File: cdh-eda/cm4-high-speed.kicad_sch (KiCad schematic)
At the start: 5 parts, among them J4 USB_OTG, U2 TPD2EUSB30ADRTR

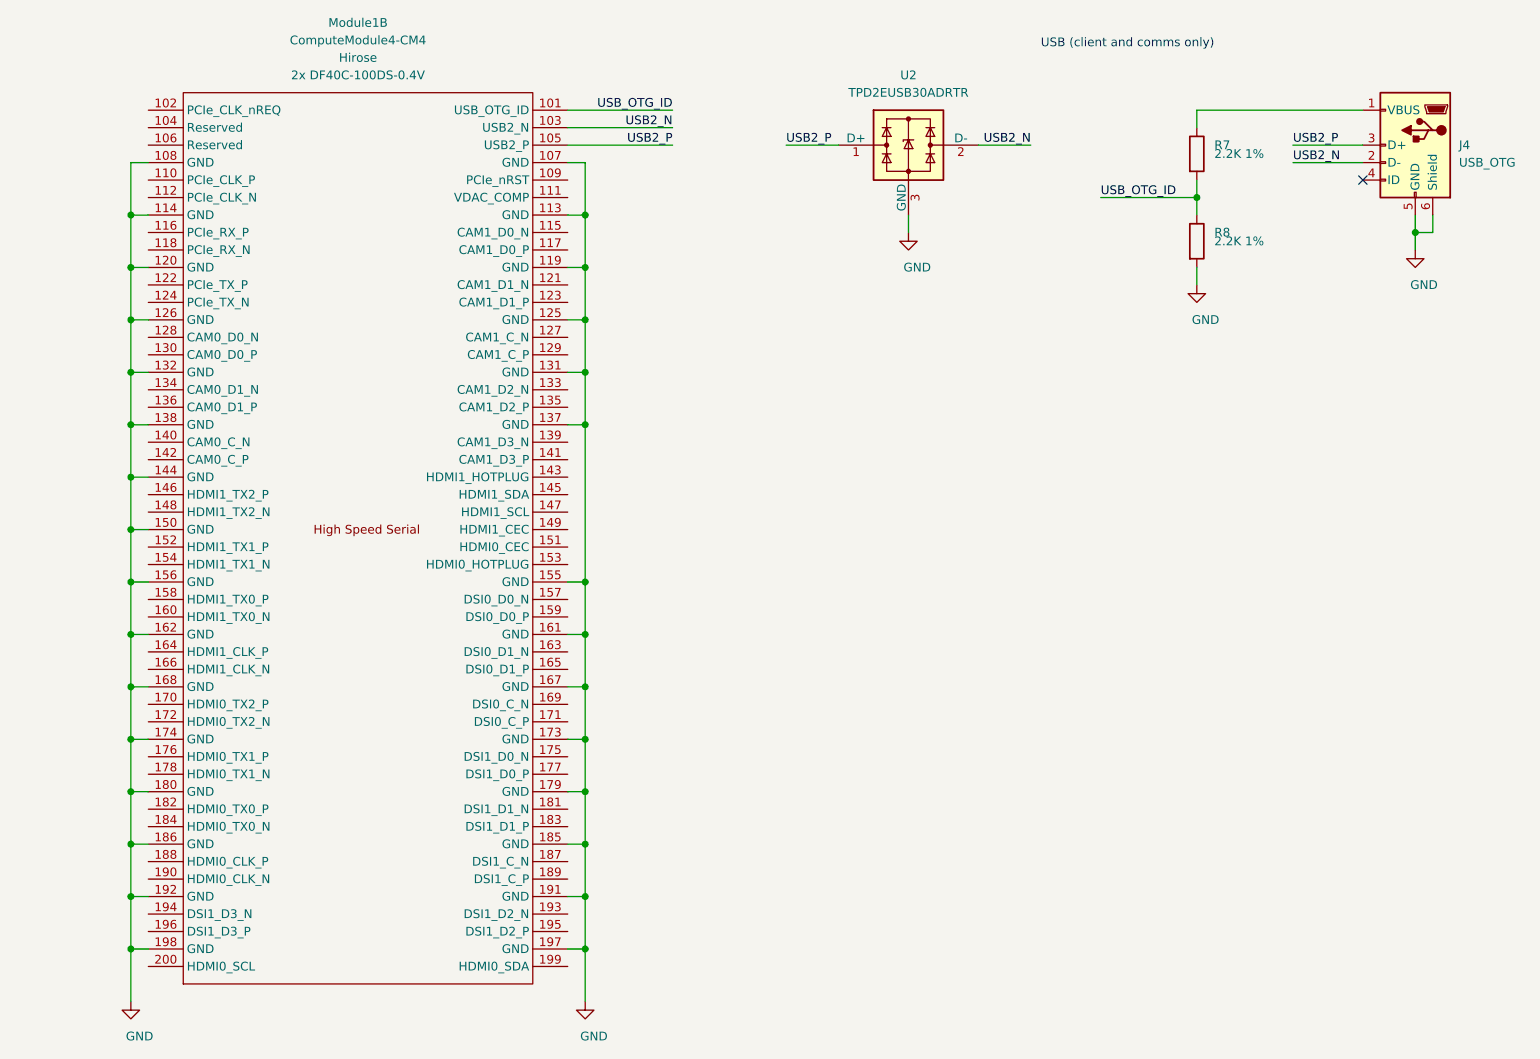
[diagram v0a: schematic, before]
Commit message: V.2 updates
 1. Add jumper CAN resistors
 2. Add camera connector
 3. Add display connector
 5. Updated CAN transceiver protective circuitry
 6. Add MCP2515 interrupt GPIO pin 18
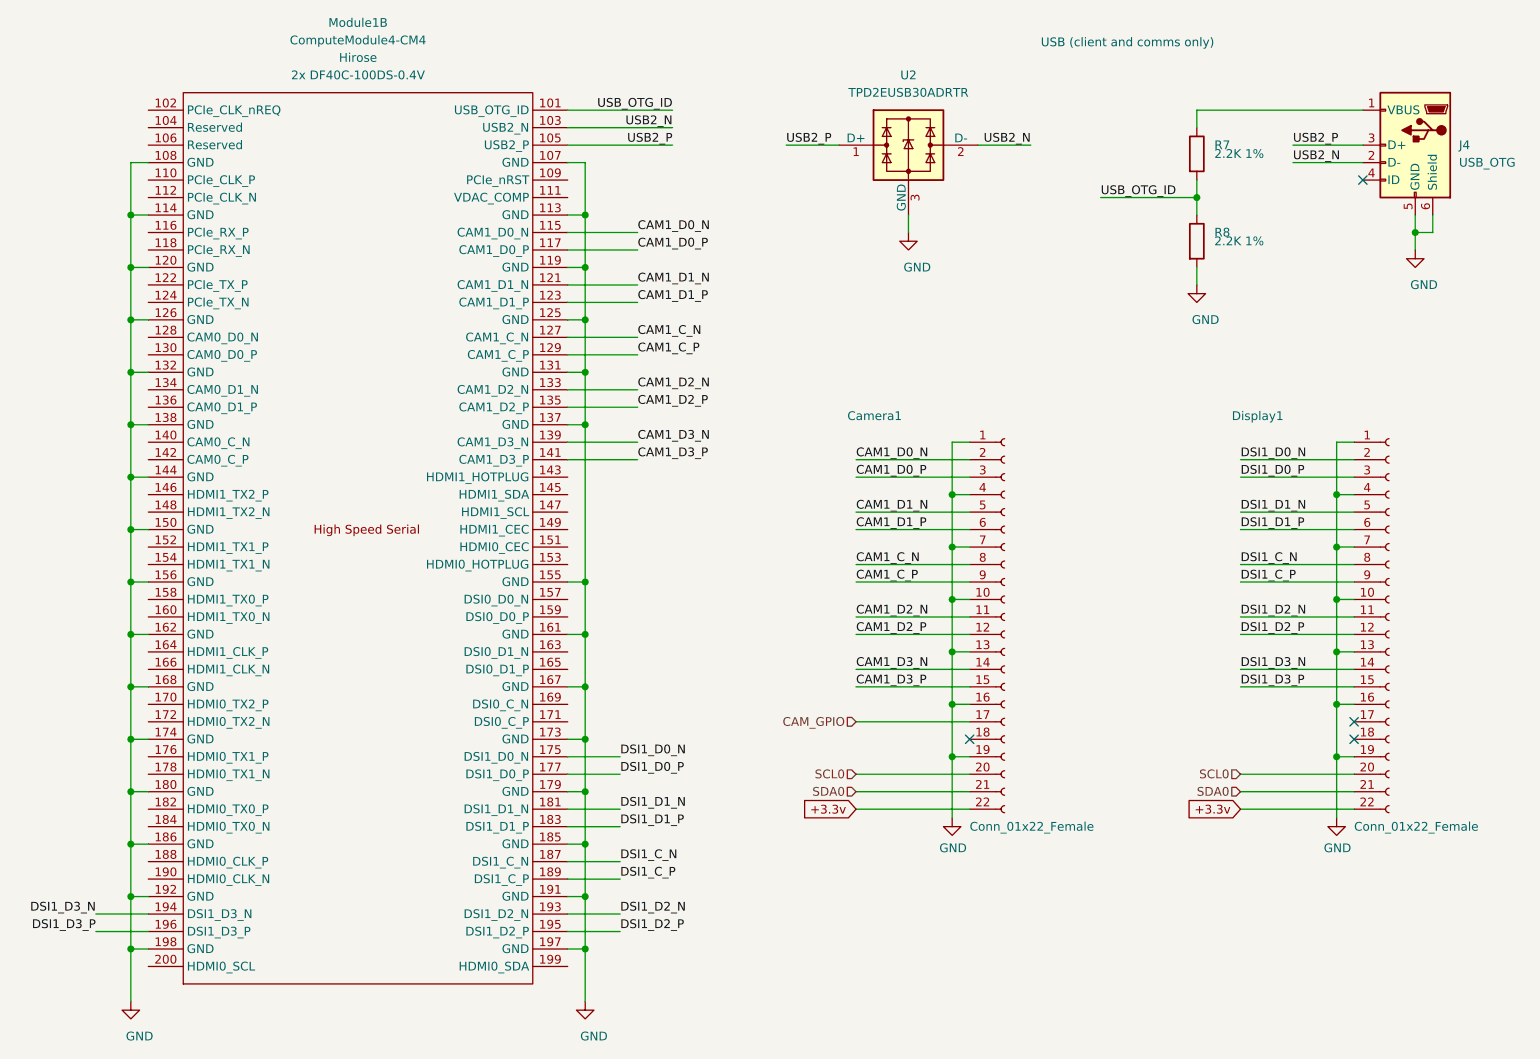
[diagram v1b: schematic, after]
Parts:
- added Camera1, Display1: Conn_01x22_Female, Connector_FFC-FPC:Hirose_FH12-22S-0.5SH_1x22-1MP_P0.50mm_Horizontal, symbol Connector:Conn_01x22_Female
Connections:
- net GND: now also Camera1.1 (Pin_1), Camera1.10 (Pin_10), Camera1.13 (Pin_13), Camera1.16 (Pin_16), Camera1.19 (Pin_19), Camera1.4 (Pin_4), Camera1.7 (Pin_7), Display1.1 (Pin_1), Display1.10 (Pin_10), Display1.13 (Pin_13), Display1.16 (Pin_16), Display1.19 (Pin_19), Display1.4 (Pin_4), Display1.7 (Pin_7)
- net CAM1_D0_N: now reaches Module1.115 (CAM1_D0_N)
- net CAM1_D0_N: now also Camera1.2 (Pin_2)
- net CAM1_D0_P: now reaches Module1.117 (CAM1_D0_P)
- net CAM1_D0_P: now also Camera1.3 (Pin_3)
- net CAM1_D1_N: now reaches Module1.121 (CAM1_D1_N)
- net CAM1_D1_N: now also Camera1.5 (Pin_5)
- net CAM1_D1_P: now reaches Module1.123 (CAM1_D1_P)
- net CAM1_D1_P: now also Camera1.6 (Pin_6)
- net CAM1_C_N: now reaches Module1.127 (CAM1_C_N)
- net CAM1_C_N: now also Camera1.8 (Pin_8)
- net CAM1_C_P: now reaches Module1.129 (CAM1_C_P)
- net CAM1_C_P: now also Camera1.9 (Pin_9)
- net CAM1_D2_N: now reaches Module1.133 (CAM1_D2_N)
- net CAM1_D2_N: now also Camera1.11 (Pin_11)
- net CAM1_D2_P: now reaches Module1.135 (CAM1_D2_P)
- net CAM1_D2_P: now also Camera1.12 (Pin_12)
- net CAM1_D3_N: now reaches Module1.139 (CAM1_D3_N)
- net CAM1_D3_N: now also Camera1.14 (Pin_14)
- net CAM1_D3_P: now reaches Module1.141 (CAM1_D3_P)
- net CAM1_D3_P: now also Camera1.15 (Pin_15)
- net DSI1_D0_N: now reaches Module1.175 (DSI1_D0_N)
- net DSI1_D0_N: now also Display1.2 (Pin_2)
- net DSI1_D0_P: now reaches Module1.177 (DSI1_D0_P)
- net DSI1_D0_P: now also Display1.3 (Pin_3)
- net DSI1_D1_N: now reaches Module1.181 (DSI1_D1_N)
- net DSI1_D1_N: now also Display1.5 (Pin_5)
- net DSI1_D1_P: now reaches Module1.183 (DSI1_D1_P)
- net DSI1_D1_P: now also Display1.6 (Pin_6)
- net DSI1_C_N: now reaches Module1.187 (DSI1_C_N)
- net DSI1_C_N: now also Display1.8 (Pin_8)
- net DSI1_C_P: now reaches Module1.189 (DSI1_C_P)
- net DSI1_C_P: now also Display1.9 (Pin_9)
- net DSI1_D2_N: now reaches Module1.193 (DSI1_D2_N)
- net DSI1_D2_N: now also Display1.11 (Pin_11)
- net DSI1_D3_N: now reaches Module1.194 (DSI1_D3_N)
- net DSI1_D3_N: now also Display1.14 (Pin_14)
- net DSI1_D2_P: now reaches Module1.195 (DSI1_D2_P)
- net DSI1_D2_P: now also Display1.12 (Pin_12)
- net DSI1_D3_P: now reaches Module1.196 (DSI1_D3_P)
- net DSI1_D3_P: now also Display1.15 (Pin_15)
- new net +3.3v: Camera1.22 (Pin_22), Display1.22 (Pin_22)
- new net CAM_GPIO: Camera1.17 (Pin_17)
- new net SCL0: Camera1.20 (Pin_20), Display1.20 (Pin_20)
- new net SDA0: Camera1.21 (Pin_21), Display1.21 (Pin_21)
- no-connect marks 1 -> 4
